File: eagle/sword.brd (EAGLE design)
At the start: 31.8 x 40.6 mm, 7 parts, among them J1 VCC_IN, J2 GND, U1 TINY45-20-DIP

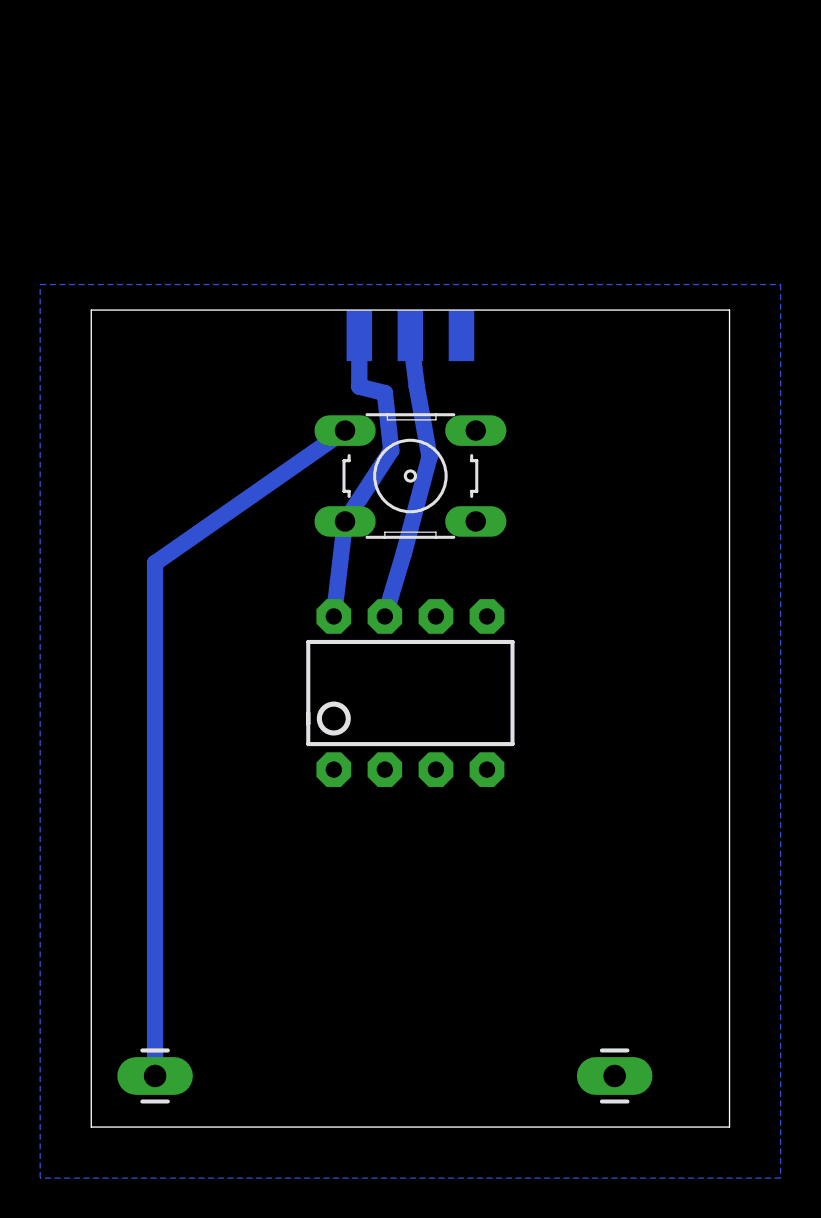
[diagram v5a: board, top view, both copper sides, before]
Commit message: complete redesign of board (super skinny so that price is cheap)
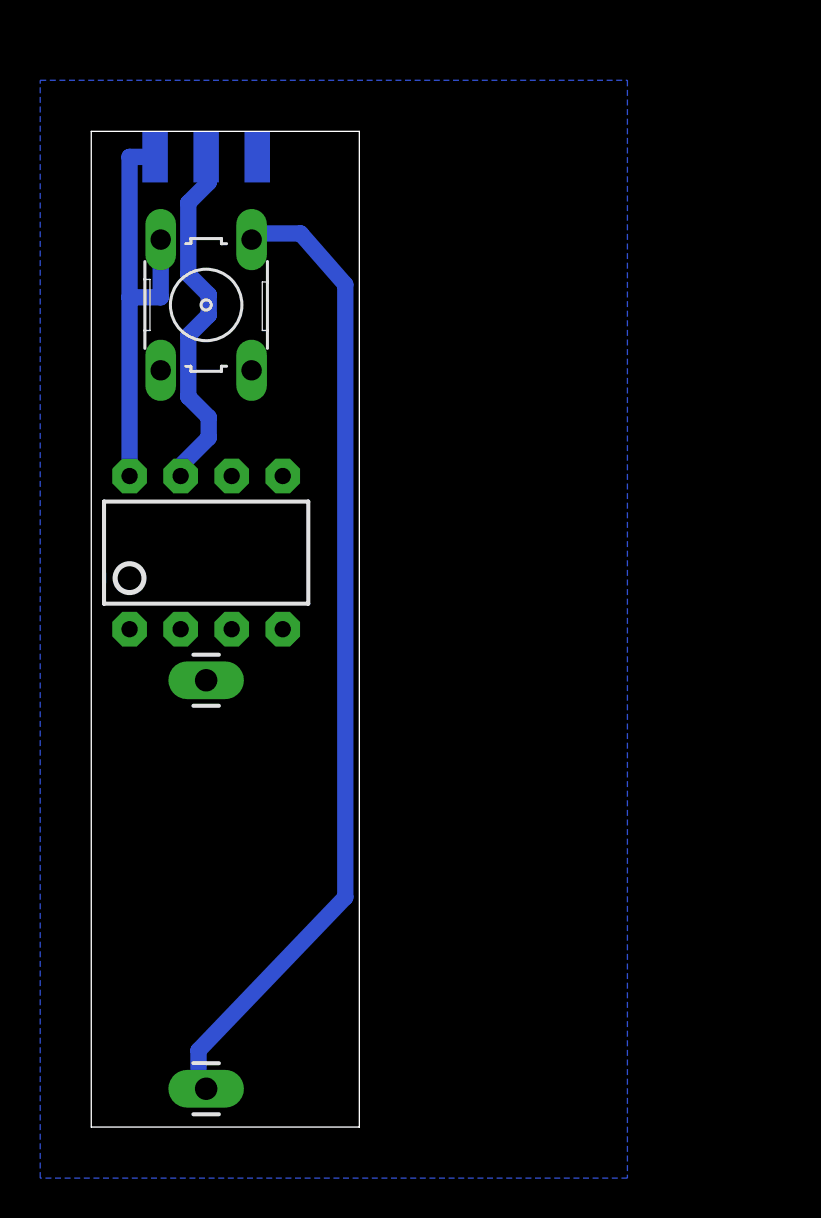
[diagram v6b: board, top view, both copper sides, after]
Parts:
- moved J2 28.3 mm to (5.71, 22.2), turned to 270 degrees
- moved PAD1 13.5 mm to (3.17, 48.3)
- moved PAD2 13.5 mm to (5.71, 48.3)
- moved PAD3 13.5 mm to (8.26, 48.3)
- moved S1 13.3 mm to (5.71, 40.9), turned to 90 degrees
- moved U1 12.3 mm to (5.71, 28.6)
- moved J1 2.62 mm to (5.71, 1.91), turned to 90 degrees
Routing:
- net VCC_SW: track 37.0 -> 49.0 mm
- net VCC: track 15.7 -> 21.6 mm
- net DIN: track 14.4 -> 18.2 mm
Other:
- board size 31.8 x 40.6 mm -> 13.3 x 49.5 mm
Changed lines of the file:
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@@
 <?xml version="1.0" encoding="utf-8"?>
 <!DOCTYPE eagle SYSTEM "eagle.dtd">
-<eagle version="8.0.0">
+<eagle version="7.5.0">
 <drawing>
 <settings>
@@
 <setting verticaltext="up"/>
 </settings>
-<grid distance="0.0125" unitdist="inch" unit="inch" style="lines" multiple="1" display="no" altdistance="0.025" altunitdist="inch" altunit="inch"/>
+<grid distance="0.025" unitdist="inch" unit="inch" style="lines" multiple="1" display="no" altdistance="0.025" altunitdist="inch" altunit="inch"/>
 <layers>
 <layer number="1" name="Top" color="4" fill="1" visible="yes" active="yes"/>
@@
 <board>
 <plain>
-<wire x1="0" y1="0" x2="31.75" y2="0" width="0" layer="20"/>
-<wire x1="31.75" y1="0" x2="31.75" y2="40.64" width="0" layer="20"/>
-<wire x1="31.75" y1="40.64" x2="0" y2="40.64" width="0" layer="20"/>
-<wire x1="0" y1="40.64" x2="0" y2="0" width="0" layer="20"/>
+<wire x1="0" y1="0" x2="13.335" y2="0" width="0" layer="20"/>
+<wire x1="13.335" y1="0" x2="13.335" y2="49.53" width="0" layer="20"/>
+<wire x1="13.335" y1="49.53" x2="0" y2="49.53" width="0" layer="20"/>
+<wire x1="0" y1="49.53" x2="0" y2="0" width="0" layer="20"/>
 </plain>
 <attributes>
@@
 </class>
 </classes>
-<designrules name="default">
+<designrules name="default *">
 <description language="de">&lt;b&gt;EAGLE Design Rules&lt;/b&gt;
 &lt;p&gt;
@@
 <param name="mdDrill" value="8mil"/>
 <param name="mdSmdStop" value="0mil"/>
-<param name="msWidth" value="10mil"/>
+<param name="msWidth" value="32mil"/>
 <param name="msDrill" value="24mil"/>
 <param name="msMicroVia" value="9.99mm"/>
@@
 <param name="RoutingGrid" value="50mil"/>
 <param name="AutoGrid" value="1"/>
-<param name="Efforts" value="0"/>
+<param name="Efforts" value="2"/>
 <param name="TopRouterVariant" value="1"/>
 <param name="tpViaShape" value="round"/>
-<param name="PrefDir.1" value="a"/>
+<param name="PrefDir.1" value="0"/>
 <param name="PrefDir.2" value="0"/>
 <param name="PrefDir.3" value="0"/>
@@
 </autorouter>
 <elements>
-<element name="J1" library="SparkFun-Connectors" package="1X01_LONGPAD" value="VCC_IN" x="3.175" y="2.54" smashed="yes" rot="R270"/>
-<element name="J2" library="SparkFun-Connectors" package="1X01_LONGPAD" value="GND" x="26.035" y="2.54" smashed="yes" rot="R90"/>
-<element name="S1" library="switch-omron" package="B3F-10XX" value="PWR_SW" x="15.875" y="32.385" smashed="yes" rot="R180">
-<attribute name="OC_NEWARK" value="36M3542" x="15.875" y="32.385" size="1.778" layer="27" rot="R180" display="off"/>
-<attribute name="MF" value="" x="15.875" y="32.385" size="1.778" layer="27" rot="R180" display="off"/>
-<attribute name="MPN" value="B3F-1000" x="15.875" y="32.385" size="1.778" layer="27" rot="R180" display="off"/>
-<attribute name="OC_FARNELL" value="176432" x="15.875" y="32.385" size="1.778" layer="27" rot="R180" display="off"/>
+<element name="J1" library="SparkFun-Connectors" package="1X01_LONGPAD" value="VCC_IN" x="5.715" y="1.905" smashed="yes" rot="R90"/>
+<element name="J2" library="SparkFun-Connectors" package="1X01_LONGPAD" value="GND" x="5.715" y="22.225" smashed="yes" rot="R270"/>
+<element name="S1" library="switch-omron" package="B3F-10XX" value="PWR_SW" x="5.715" y="40.894" smashed="yes" rot="R90">
+<attribute name="OC_NEWARK" value="36M3542" x="5.715" y="40.894" size="1.778" layer="27" rot="R90" display="off"/>
+<attribute name="MF" value="" x="5.715" y="40.894" size="1.778" layer="27" rot="R90" display="off"/>
+<attribute name="MPN" value="B3F-1000" x="5.715" y="40.894" size="1.778" layer="27" rot="R90" display="off"/>
+<attribute name="OC_FARNELL" value="176432" x="5.715" y="40.894" size="1.778" layer="27" rot="R90" display="off"/>
 </element>
-<element name="U1" library="SparkFun-DigitalIC" package="DIP08" value="TINY45-20-DIP" x="15.875" y="21.59" smashed="yes">
-<attribute name="PROD_ID" value="IC-09439" x="15.875" y="21.59" size="1.778" layer="27" display="off"/>
+<element name="U1" library="SparkFun-DigitalIC" package="DIP08" value="TINY45-20-DIP" x="5.715" y="28.575" smashed="yes">
+<attribute name="PROD_ID" value="IC-09439" x="5.715" y="28.575" size="1.778" layer="27" display="off"/>
 </element>
-<element name="PAD1" library="wirepad" package="SMD1,27-2,54" value="NEO_VCC" x="13.335" y="39.37" smashed="yes" rot="MR0">
-<attribute name="VALUE" x="13.335" y="39.37" size="0.0254" layer="28" rot="MR0"/>
+<element name="PAD1" library="wirepad" package="SMD1,27-2,54" value="NEO_VCC" x="3.175" y="48.26" smashed="yes" rot="MR0">
+<attribute name="VALUE" x="3.175" y="48.26" size="0.0254" layer="28" rot="MR0"/>
 </element>
-<element name="PAD2" library="wirepad" package="SMD1,27-2,54" value="NEO_DIN" x="15.875" y="39.37" smashed="yes" rot="MR0">
-<attribute name="VALUE" x="15.875" y="39.37" size="0.0254" layer="28" rot="MR0"/>
+<element name="PAD2" library="wirepad" package="SMD1,27-2,54" value="NEO_DIN" x="5.715" y="48.26" smashed="yes" rot="MR0">
+<attribute name="VALUE" x="5.715" y="48.26" size="0.0254" layer="28" rot="MR0"/>
 </element>
-<element name="PAD3" library="wirepad" package="SMD1,27-2,54" value="NEO_GND" x="18.415" y="39.37" smashed="yes" rot="MR0">
-<attribute name="VALUE" x="18.415" y="39.37" size="0.0254" layer="28" rot="MR0"/>
+<element name="PAD3" library="wirepad" package="SMD1,27-2,54" value="NEO_GND" x="8.255" y="48.26" smashed="yes" rot="MR0">
+<attribute name="VALUE" x="8.255" y="48.26" size="0.0254" layer="28" rot="MR0"/>
 </element>
 </elements>
@@
 <contactref element="U1" pad="8"/>
 <contactref element="S1" pad="2"/>
-<wire x1="12.6238" y1="30.1244" x2="12.065" y2="25.4" width="0.8128" layer="16"/>
 <contactref element="PAD1" pad="1"/>
-<wire x1="13.335" y1="39.37" x2="13.335" y2="36.83" width="0.8128" layer="16"/>
-<wire x1="13.335" y1="36.83" x2="14.605" y2="36.5125" width="0.8128" layer="16"/>
-<wire x1="14.605" y1="36.5125" x2="14.9225" y2="33.655" width="0.8128" layer="16"/>
-<wire x1="14.9225" y1="33.655" x2="12.6238" y2="30.1244" width="0.8128" layer="16"/>
+<wire x1="1.905" y1="32.385" x2="1.905" y2="41.275" width="0.8128" layer="16"/>
+<wire x1="1.905" y1="41.275" x2="1.905" y2="48.26" width="0.8128" layer="16"/>
+<wire x1="1.905" y1="48.26" x2="3.175" y2="48.26" width="0.8128" layer="16"/>
+<wire x1="3.4544" y1="44.1452" x2="3.4544" y2="41.275" width="0.8128" layer="16"/>
+<wire x1="3.4544" y1="41.275" x2="1.905" y2="41.275" width="0.8128" layer="16"/>
 </signal>
 <signal name="GND">
@@
 <contactref element="J2" pad="1"/>
 <polygon width="1.27" layer="16" thermals="no">
-<vertex x="-2.54" y="41.91"/>
-<vertex x="34.29" y="41.91"/>
-<vertex x="34.29" y="-2.54"/>
+<vertex x="-2.54" y="52.07"/>
+<vertex x="26.67" y="52.07"/>
+<vertex x="26.67" y="-2.54"/>
 <vertex x="-2.54" y="-2.54"/>
 </polygon>
@@
 <contactref element="U1" pad="7"/>
 <contactref element="PAD2" pad="1"/>
-<wire x1="15.5575" y1="28.575" x2="14.605" y2="25.4" width="0.8128" layer="16"/>
-<wire x1="15.875" y1="39.37" x2="16.1925" y2="36.83" width="0.8128" layer="16"/>
-<wire x1="16.1925" y1="36.83" x2="16.8275" y2="33.3375" width="0.8128" layer="16"/>
-<wire x1="16.8275" y1="33.3375" x2="15.5575" y2="28.575" width="0.8128" layer="16"/>
+<wire x1="5.842" y1="46.99" x2="5.842" y2="48.006" width="0.8128" layer="16"/>
+<wire x1="4.826" y1="45.974" x2="5.842" y2="46.99" width="0.8128" layer="16"/>
+<wire x1="4.826" y1="42.418" x2="4.826" y2="45.974" width="0.8128" layer="16"/>
+<wire x1="5.842" y1="41.402" x2="4.826" y2="42.418" width="0.8128" layer="16"/>
+<wire x1="5.842" y1="40.386" x2="5.842" y2="41.402" width="0.8128" layer="16"/>
+<wire x1="4.826" y1="39.37" x2="5.842" y2="40.386" width="0.8128" layer="16"/>
+<wire x1="4.826" y1="36.322" x2="4.826" y2="39.37" width="0.8128" layer="16"/>
+<wire x1="5.842" y1="35.306" x2="4.826" y2="36.322" width="0.8128" layer="16"/>
+<wire x1="5.842" y1="34.29" x2="5.842" y2="35.306" width="0.8128" layer="16"/>
+<wire x1="4.318" y1="32.766" x2="5.842" y2="34.29" width="0.8128" layer="16"/>
+<wire x1="5.842" y1="48.006" x2="5.715" y2="48.26" width="0.8128" layer="16"/>
+<wire x1="4.318" y1="32.766" x2="4.445" y2="32.385" width="0.8128" layer="16"/>
 </signal>
 <signal name="VCC_SW">
 <contactref element="J1" pad="1"/>
 <contactref element="S1" pad="4"/>
-<wire x1="12.6238" y1="34.6456" x2="3.175" y2="28.0543" width="0.8128" layer="16"/>
-<wire x1="3.175" y1="28.0543" x2="3.175" y2="2.54" width="0.8128" layer="16"/>
+<wire x1="10.414" y1="44.45" x2="8.382" y2="44.45" width="0.8128" layer="16"/>
+<wire x1="12.6365" y1="41.91" x2="10.414" y2="44.45" width="0.8128" layer="16"/>
+<wire x1="12.6365" y1="11.43" x2="12.6365" y2="41.91" width="0.8128" layer="16"/>
+<wire x1="5.334" y1="3.81" x2="12.6365" y2="11.43" width="0.8128" layer="16"/>
+<wire x1="5.334" y1="2.286" x2="5.334" y2="3.81" width="0.8128" layer="16"/>
+<wire x1="8.382" y1="44.45" x2="7.9756" y2="44.1452" width="0.8128" layer="16"/>
+<wire x1="5.334" y1="2.286" x2="5.715" y2="1.905" width="0.8128" layer="16"/>
 </signal>
 </signals>

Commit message: swapped battery around
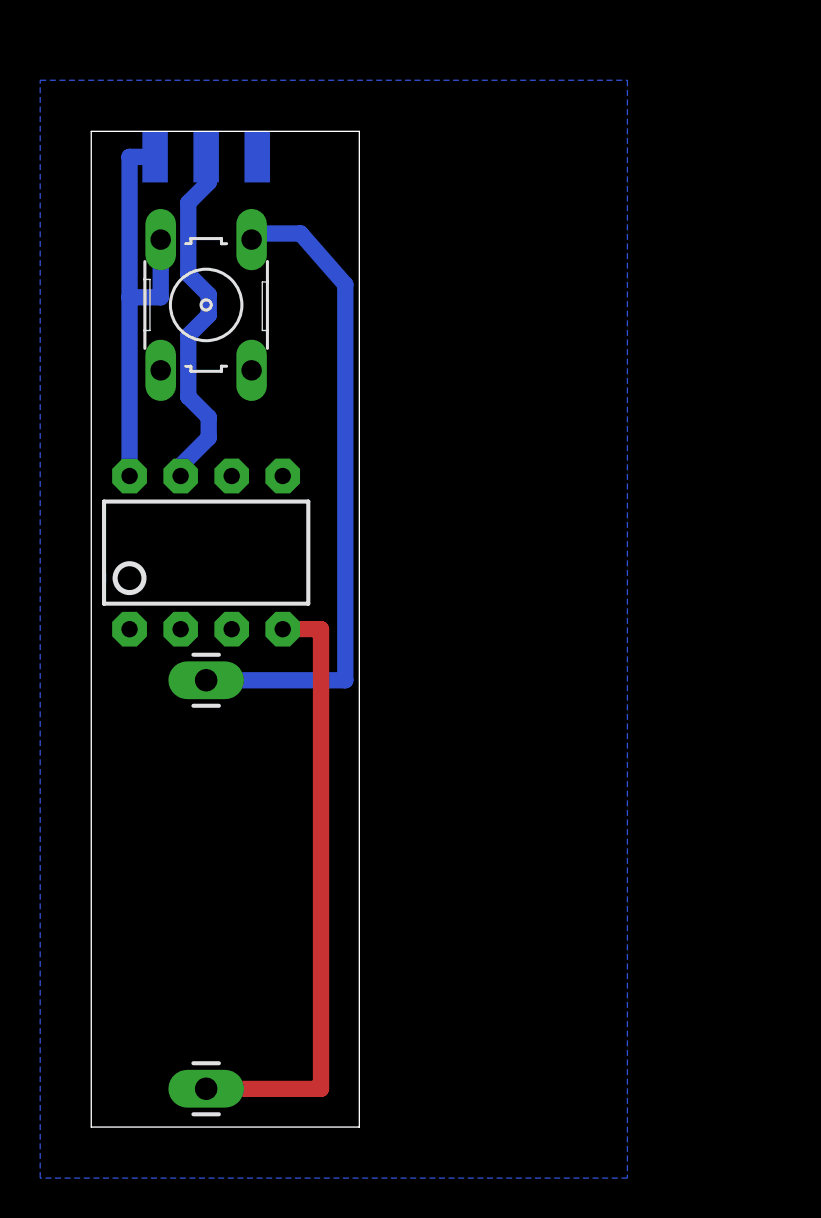
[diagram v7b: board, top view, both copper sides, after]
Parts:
- moved J1 20.3 mm to (5.71, 22.2)
- moved J2 20.3 mm to (5.71, 1.91)
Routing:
- net GND: track 0.00 -> 30.5 mm
- net VCC_SW: track 49.0 -> 32.5 mm
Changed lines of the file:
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@@
 <?xml version="1.0" encoding="utf-8"?>
 <!DOCTYPE eagle SYSTEM "eagle.dtd">
-<eagle version="7.5.0">
+<eagle version="8.0.2">
 <drawing>
 <settings>
@@
 </autorouter>
 <elements>
-<element name="J1" library="SparkFun-Connectors" package="1X01_LONGPAD" value="VCC_IN" x="5.715" y="1.905" smashed="yes" rot="R90"/>
-<element name="J2" library="SparkFun-Connectors" package="1X01_LONGPAD" value="GND" x="5.715" y="22.225" smashed="yes" rot="R270"/>
+<element name="J1" library="SparkFun-Connectors" package="1X01_LONGPAD" value="VCC_IN" x="5.715" y="22.225" smashed="yes" rot="R90"/>
+<element name="J2" library="SparkFun-Connectors" package="1X01_LONGPAD" value="GND" x="5.715" y="1.905" smashed="yes" rot="R270"/>
 <element name="S1" library="switch-omron" package="B3F-10XX" value="PWR_SW" x="5.715" y="40.894" smashed="yes" rot="R90">
-<attribute name="OC_NEWARK" value="36M3542" x="5.715" y="40.894" size="1.778" layer="27" rot="R90" display="off"/>
 <attribute name="MF" value="" x="5.715" y="40.894" size="1.778" layer="27" rot="R90" display="off"/>
 <attribute name="MPN" value="B3F-1000" x="5.715" y="40.894" size="1.778" layer="27" rot="R90" display="off"/>
 <attribute name="OC_FARNELL" value="176432" x="5.715" y="40.894" size="1.778" layer="27" rot="R90" display="off"/>
+<attribute name="OC_NEWARK" value="36M3542" x="5.715" y="40.894" size="1.778" layer="27" rot="R90" display="off"/>
 </element>
 <element name="U1" library="SparkFun-DigitalIC" package="DIP08" value="TINY45-20-DIP" x="5.715" y="28.575" smashed="yes">
@@
 </polygon>
 <contactref element="PAD3" pad="1"/>
+<wire x1="5.715" y1="1.905" x2="11.43" y2="1.905" width="0.8128" layer="1"/>
+<wire x1="11.43" y1="1.905" x2="11.43" y2="24.765" width="0.8128" layer="1"/>
+<wire x1="11.43" y1="24.765" x2="9.525" y2="24.765" width="0.8128" layer="1"/>
 </signal>
 <signal name="DIN">
@@
 <wire x1="10.414" y1="44.45" x2="8.382" y2="44.45" width="0.8128" layer="16"/>
 <wire x1="12.6365" y1="41.91" x2="10.414" y2="44.45" width="0.8128" layer="16"/>
-<wire x1="12.6365" y1="11.43" x2="12.6365" y2="41.91" width="0.8128" layer="16"/>
-<wire x1="5.334" y1="3.81" x2="12.6365" y2="11.43" width="0.8128" layer="16"/>
-<wire x1="5.334" y1="2.286" x2="5.334" y2="3.81" width="0.8128" layer="16"/>
 <wire x1="8.382" y1="44.45" x2="7.9756" y2="44.1452" width="0.8128" layer="16"/>
-<wire x1="5.334" y1="2.286" x2="5.715" y2="1.905" width="0.8128" layer="16"/>
+<wire x1="5.715" y1="22.225" x2="12.6365" y2="22.225" width="0.8128" layer="16"/>
+<wire x1="12.6365" y1="22.225" x2="12.6365" y2="41.91" width="0.8128" layer="16"/>
 </signal>
 </signals>
